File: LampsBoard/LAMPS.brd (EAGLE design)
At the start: 101.6 x 53.3 mm, 49 parts, among them IC1 LM358N, IC2 LM358N, IC3 5V, IC4 78L12Z, IC5 78L12Z, Q1 TIP120

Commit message: More work...
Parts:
- removed IC2: LM358N, linear:DIL08
- removed U$3: FIDUCIALMOUNT, SmartPrj:FIDUCIA-MOUNT
- removed X, Y: (no value), pinhead:1X01
- added 12V-AUX: (no value), SparkFun:1X02
- added 3.3V, 5V, VCC: (no value), adafruit:1X01
- added ADCH1: 8-15, pinhead:1X08
- added AUX1, COMM: 14-21, pinhead:1X08
- added F3: MFR500, RepRapjr:MFR500
- added IC6: UA741P, linear:DIL08
- added JP7: 22-37, pinhead:2X08
- added R4, R5, R6, R7: 5K, SparkFun:AXIAL-0.3
- added S2: (no value), switch-omron:B3F-31XX
- added X-GALVO, Y-GALVO: 22-23-2031, con-molex:22-23-2031
- added X1: MSTBA2, con-phoenix-508:MSTBA2
- IC1: value LM358N -> UA741P
- moved IC1 18.4 mm to (45.1, 27.3), turned to 270 degrees
- moved C6 10.8 mm to (62.9, 18.4)
- moved IC5 10.2 mm to (18.4, 17.1)
- moved C7 10.2 mm to (57.8, 23.5)
- moved C4 6.75 mm to (52.1, 24.8), turned to 270 degrees
- moved C14 6.25 mm to (12.7, 16.5)
- moved C3 3.81 mm to (57.1, 29.8)
- moved C13 1.91 mm to (12.7, 21.6)
- moved Z-MOT 1.91 mm to (76.2, 19.1)
- moved C12 1.27 mm to (12.7, 26.7)
- moved C1 1.27 mm to (57.1, 41.3)
- moved C2 0.63 mm to (57.1, 35.6), turned to 0 degrees
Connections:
- removed net V+: IC1.8, IC2.8
- removed net V-: IC1.4, IC2.4
- new net +12V: 12V-AUX.1, C10.1, C12.1, C13.1, F3.1, IC3.IN, IC4.3, IC5.3, Z-AXIS.VMOT
- new net N$27: IC6.4, X-GALVO.3
- new net N$28: IC6.7, X-GALVO.1
- new net N$29: COMM.2, COMMUNICATION.2
- new net N$30: R7.P$1
- new net N$31: IC1.6, R6.P$2, Y-GALVO.2
- new net N$32: IC1.4, Y-GALVO.3
- new net N$33: IC1.7, Y-GALVO.1
- new net N$34: IC1.3
- new net N$35: COMM.3, COMMUNICATION.3
- new net N$36: F3.2, X1.1
- new net N$37: COMM.4, COMMUNICATION.4
- new net N$38: COMM.5
- new net N$39: COMM.6, COMMUNICATION.6
- new net N$40: COMM.7, COMMUNICATION.7
- new net N$41: COMM.8, COMMUNICATION.8
- new net N$42: ADCH.1, ADCH1.1
- new net N$43: ADCH1.2
- new net N$44: ADCH.3, ADCH1.3
- new net N$45: ADCH.4, ADCH1.4
- new net N$46: ADCH.5, ADCH1.5
- new net N$47: ADCH.6, ADCH1.6
- new net N$48: ADCH.7, ADCH1.7
- new net N$49: ADCH.8, ADCH1.8
- new net N$50: JP1.15, JP7.15
- new net N$51: JP1.16, JP7.16
- new net N$52: JP1.13, JP7.13
- new net N$53: JP1.14, JP7.14
- new net N$54: JP1.11, JP7.11
- new net N$55: JP1.12, JP7.12
- new net N$56: JP1.9, JP7.9
- new net N$57: JP1.10, JP7.10
- new net N$58: JP1.7, JP7.7
- new net N$59: JP1.8, JP7.8
- new net N$60: JP1.5, JP7.5
- new net N$61: JP1.6, JP7.6
- new net N$62: JP1.3, JP7.3
- new net N$63: JP1.4, JP7.4
- new net N$64: JP1.1, JP7.1
- new net N$65: JP1.2, JP7.2
- new net N$74: AUX1.1, PWML.1
- new net N$75: AUX1.2, PWML.2
- new net N$76: AUX1.3, PWML.3
- new net N$77: AUX1.4, PWML.4
- new net N$78: AUX1.5, PWML.5
- new net N$79: AUX1.6, PWML.6
- new net N$80: AUX1.7, PWML.7
- new net RESET: POWER.1, S2.2
- net GND: now also 12V-AUX.2, AUX1.8, IC1.2, IC6.2, POWER.4, POWER.5, R4.P$1, R5.P$2, R6.P$1, R7.P$2, S2.1, X1.2
- net N$10: now also 5V.1, POWER.3; no longer IC2.1, IC2.2, Y.1
- net N$5: now also IC6.3; no longer IC1.3
- net N$6: now also R5.P$1
- net N$7: now also IC6.6, R4.P$2, X-GALVO.2; no longer IC1.1, IC1.2, X.1
- net N$8: now also 3.3V.1, POWER.2; no longer AD420ARZ1.17, IC2.3
- net N$9: now also COMM.1, COMMUNICATION.1; no longer AD420ARZ1.14, AD420ARZ1.15
- net VCC: now also VCC.1; no longer C10.1, C12.1, C13.1, IC3.IN, IC4.3, IC5.3, Z-AXIS.VMOT
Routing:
- net +12V: track 0.00 -> 155.7 mm
- net N$52: track 0.00 -> 100.1 mm, vias 0 -> 2
- net N$56: track 0.00 -> 78.8 mm, vias 0 -> 2
- net N$28: track 0.00 -> 68.6 mm
- net N$58: track 0.00 -> 68.1 mm
- net N$60: track 0.00 -> 67.5 mm, vias 0 -> 1
- net N$31: track 0.00 -> 59.8 mm, vias 0 -> 1
- net N$33: track 0.00 -> 51.5 mm, vias 0 -> 1
- net VCC: track 185.4 -> 136.3 mm, vias 0 -> 2
- net N$10: track 45.8 -> 5.08 mm, vias 1 -> 0
- net N$32: track 0.00 -> 35.5 mm
- net N$8: track 20.7 -> 55.2 mm, vias 0 -> 1
- net N$27: track 0.00 -> 33.8 mm
- net N$54: track 0.00 -> 27.8 mm, vias 0 -> 1
- net N$36: track 0.00 -> 19.9 mm, vias 0 -> 1
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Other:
- outline, holes or cut-outs redrawn
- board text removed: "22"
- board text removed: "24"
- board text removed: "26"
- board text removed: "28"
- board text removed: "30"
- board text removed: "31"
- board text removed: "32"
- board text removed: "33"
- board text removed: "34"
- board text removed: "35"
- board text removed: "36"
- board text removed: "37"
- board text removed: "38"
- board text removed: "39"
- board text removed: "40"
- board text removed: "41"
- board text removed: "42"
- board text removed: "43"
- board text removed: "44"
- board text removed: "45"
- board text removed: "46"
- board text removed: "47"
- board text removed: "48"
- board text removed: "49"
- board text removed: "50"
- board text removed: "51"
- board text removed: "52"
- board text removed: "53"
- board text removed: "ANALOG IN"
- board text removed: "DIGITAL"
- board text removed: "Galvos"
- board text removed: "PWM"
- board text removed: "RX1"
- board text removed: "RX2"
- board text removed: "RX3"
- board text removed: "SDA"
- board text removed: "TX1"
- board text removed: "TX2"
- board text removed: "TX3"

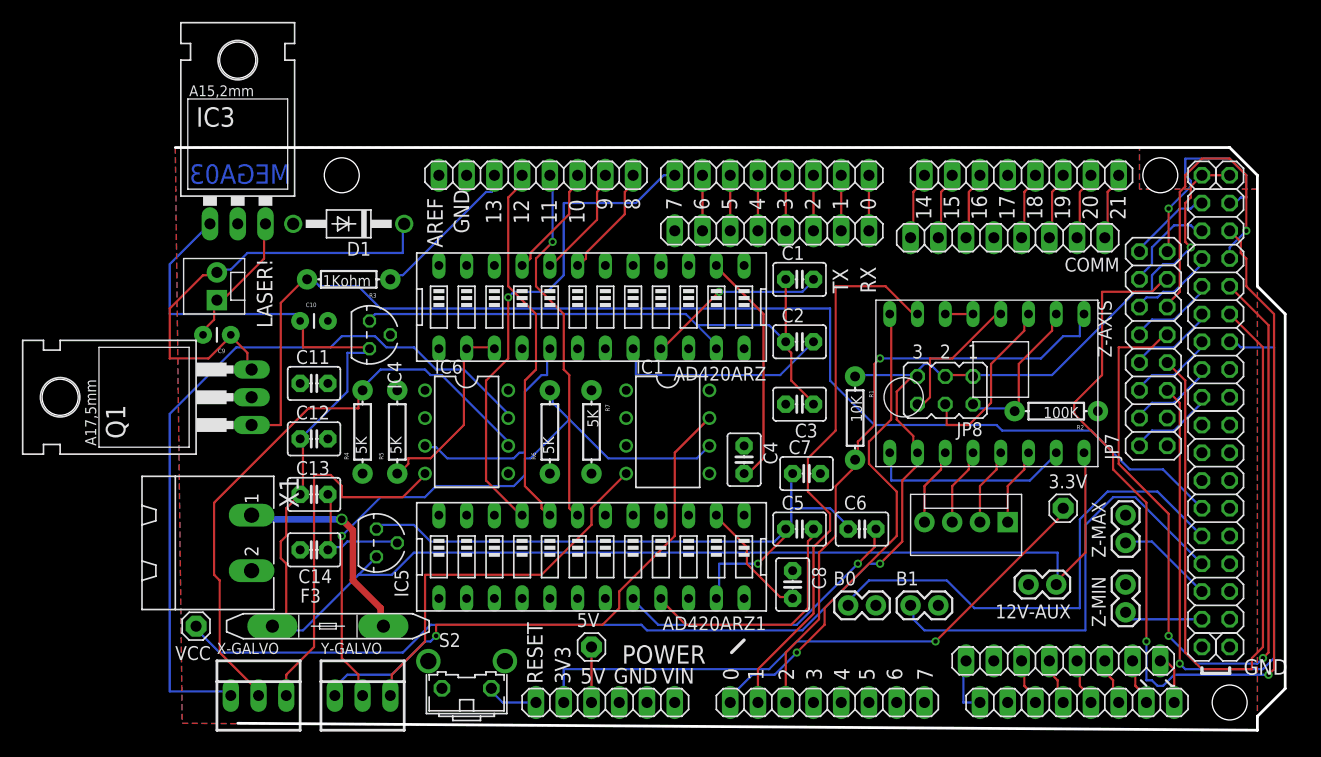
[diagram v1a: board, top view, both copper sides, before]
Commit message: Switching AD420 Chip mount
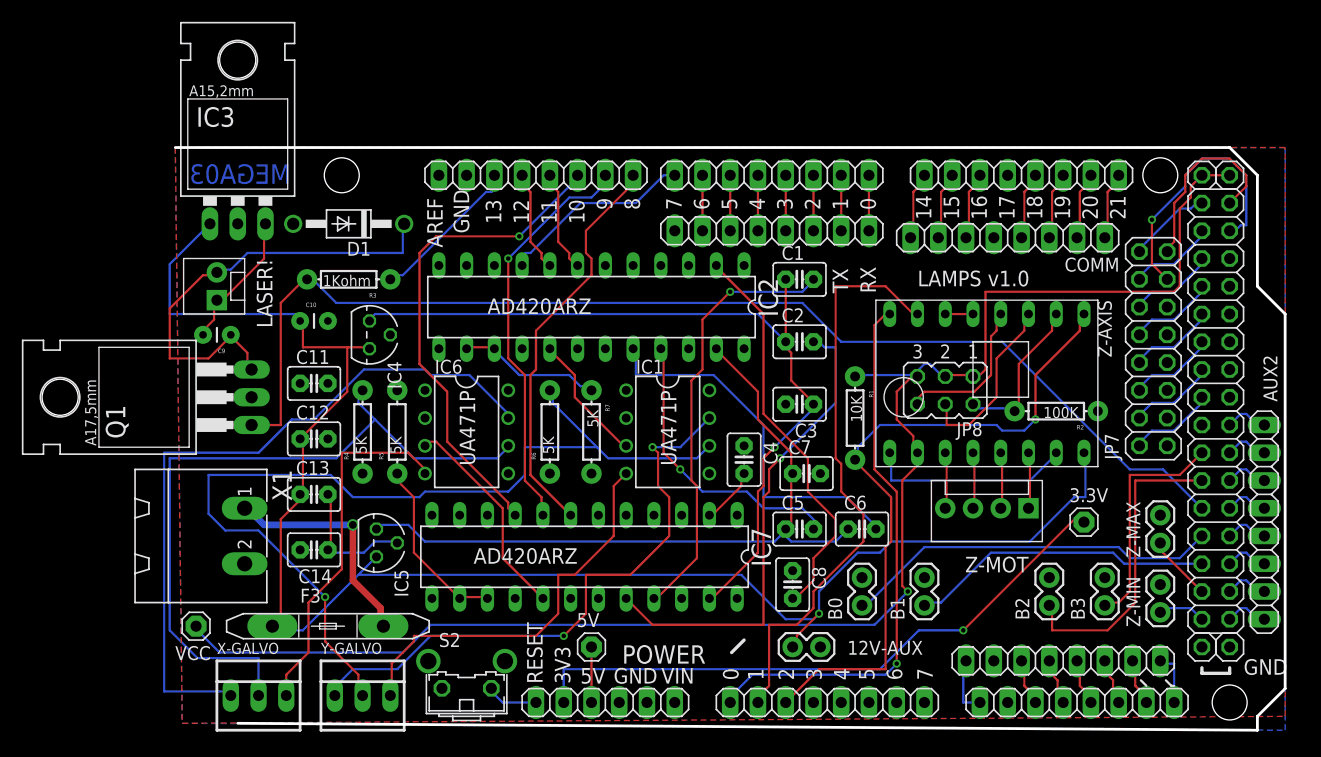
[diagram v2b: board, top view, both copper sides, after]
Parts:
- removed AD420ARZ, AD420ARZ1: (no value), special:EDG-12
- added AUX2: 14-21, pinhead:1X08
- added B2, B3: (no value), SparkFun:1X02
- added IC2, IC7: AD420ARZ, ic-package:DIL24-3
- moved 12V-AUX 24.8 mm to (56.5, 7.62), turned to 0 degrees
- moved Z-MAX 3.17 mm to (90.2, 17.1)
- moved Z-MIN 3.17 mm to (90.2, 10.8)
- moved 3.3V 2.29 mm to (83.2, 19.1)
- moved Z-MOT 2.29 mm to (78.1, 20.3)
- moved B0 1.27 mm to (62.9, 11.4), turned to 90 degrees
- moved B1 1.27 mm to (68.6, 11.4), turned to 90 degrees
- moved X1 0.90 mm to (1.27, 17.8)
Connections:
- new net D40: B3.1, JP2.14
- new net D42: B2.1, JP2.12
- new net N$66: AUX2.1, JP2.15
- new net N$67: AUX2.2, JP2.13
- new net N$68: AUX2.3, JP2.11
- new net N$69: AUX2.4, JP2.9
- new net N$70: AUX2.5, JP2.7
- new net N$71: AUX2.6, JP2.5
- new net N$72: AUX2.7, JP2.3
- new net N$73: AUX2.8, JP2.1
- net D10: now also IC7.9; no longer AD420ARZ.9
- net D11: now also IC2.7; no longer AD420ARZ1.7
- net D12: now also IC2.8; no longer AD420ARZ1.8
- net D7: now also IC2.9; no longer AD420ARZ1.9
- net D8: now also IC7.7; no longer AD420ARZ.7
- net D9: now also IC7.8; no longer AD420ARZ.8
- net GND: now also B2.2, B3.2, IC2.11, IC2.4, IC2.5, IC2.6, IC7.11, IC7.4, IC7.5, IC7.6; no longer AD420ARZ.11, AD420ARZ.4, AD420ARZ.5, AD420ARZ.6, AD420ARZ1.11, AD420ARZ1.4, AD420ARZ1.5, AD420ARZ1.6
- net N$1: now also IC2.21; no longer AD420ARZ1.21
- net N$18: now also IC7.23; no longer AD420ARZ.23
- net N$19: now also IC7.2; no longer AD420ARZ.2
- net N$2: now also IC2.20; no longer AD420ARZ1.20
- net N$24: now also IC2.2; no longer AD420ARZ1.2
- net N$25: now also IC2.23; no longer AD420ARZ1.23
- net N$3: now also IC7.21; no longer AD420ARZ.21
- net N$30: now also IC2.14, IC2.15
- net N$34: now also IC2.17
- net N$4: now also IC7.20; no longer AD420ARZ.20
- net N$5: now also IC7.17; no longer AD420ARZ.17
- net N$6: now also IC7.14, IC7.15; no longer AD420ARZ.14, AD420ARZ.15
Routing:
- net N$56: track 78.8 -> 0.00 mm, vias 2 -> 0
- net N$52: track 100.1 -> 24.5 mm, vias 2 -> 1
- net N$58: track 68.1 -> 0.00 mm
- net N$60: track 67.5 -> 0.00 mm, vias 1 -> 0
- net D10: track 10.6 -> 45.6 mm, vias 0 -> 1
- net D42: track 0.00 -> 28.3 mm
- net D7: track 45.9 -> 18.0 mm, vias 1 -> 0
- net N$54: track 27.8 -> 0.00 mm, vias 1 -> 0
- net D9: track 10.6 -> 37.5 mm, vias 0 -> 1
- net D8: track 10.6 -> 37.1 mm
- net N$31: track 59.8 -> 85.8 mm
- net N$24: track 11.1 -> 36.7 mm
- net D12: track 34.3 -> 9.51 mm
- net D11: track 33.6 -> 9.51 mm, vias 1 -> 0
- net N$4: track 20.0 -> 44.0 mm, vias 0 -> 1
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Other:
- board text added: "AD420ARZ"
- board text added: "LAMPS v1.0"
- board text added: "UA471P"
- board text added: "Z-MOT"

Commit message: movin
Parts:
- removed JP7: 22-37, pinhead:2X08
- removed X1: MSTBA2, con-phoenix-508:MSTBA2
- added 12V: MSTBA2, con-phoenix-508:MSTBA2
- IC2, IC7: value AD420ARZ -> (none); device ic-package:DIL24-3 -> ic-package:DIL24-6
- moved 12V-AUX 54.9 mm to (1.91, 1.91), turned to 90 degrees
- moved 5V 50.9 mm to (88.9, 10.8)
- moved IC6 42.6 mm to (68.6, 19.7), turned to 0 degrees
- moved IC1 37.0 mm to (81.3, 19.7), turned to 0 degrees
- moved C7 30.8 mm to (27.3, 19.1)
- moved C5 30.4 mm to (27.3, 24.1)
- moved C8 29.2 mm to (27.3, 12.7), turned to 180 degrees
- moved 3.3V 28.6 mm to (81.3, 47.6), turned to 180 degrees
- moved C4 27.2 mm to (68.6, 46.4), turned to 180 degrees
- moved Z-MOT 19.7 mm to (88.9, 36.8), turned to 270 degrees
- moved C6 18.3 mm to (56.5, 35.6), turned to 270 degrees
- moved R7 17.9 mm to (22.2, 19.1)
- moved R6 17.5 mm to (22.2, 40.0), turned to 270 degrees
- moved R1 16.9 mm to (78.7, 32.4), turned to 0 degrees
- moved Z-MIN 8.28 mm to (90.8, 19.1), turned to 180 degrees
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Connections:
- removed net N$50: JP1.15, JP7.15
- removed net N$51: JP1.16, JP7.16
- removed net N$52: JP1.13, JP7.13
- removed net N$53: JP1.14, JP7.14
- removed net N$54: JP1.11, JP7.11
- removed net N$55: JP1.12, JP7.12
- removed net N$56: JP1.9, JP7.9
- removed net N$57: JP1.10, JP7.10
- removed net N$58: JP1.7, JP7.7
- removed net N$59: JP1.8, JP7.8
- removed net N$60: JP1.5, JP7.5
- removed net N$61: JP1.6, JP7.6
- removed net N$62: JP1.3, JP7.3
- removed net N$63: JP1.4, JP7.4
- removed net N$64: JP1.1, JP7.1
- removed net N$65: JP1.2, JP7.2
- net GND: now also 12V.2; no longer X1.2
- net N$36: now also 12V.1; no longer X1.1
- net N$38: now also COMMUNICATION.5
- net N$43: now also ADCH.2
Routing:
- net N$34: track 12.0 -> 66.6 mm, vias 0 -> 2
- net N$10: track 5.08 -> 55.8 mm
- net N$33: track 54.6 -> 100.5 mm, vias 2 -> 1
- net N$32: track 36.7 -> 78.5 mm
- net N$27: track 33.0 -> 66.8 mm, vias 0 -> 3
- net N$7: track 66.4 -> 97.4 mm, vias 0 -> 1
- net N$52: track 24.5 -> 0.00 mm, vias 1 -> 0
- net N$19: track 5.29 -> 27.9 mm
- net N$23: track 5.33 -> 24.6 mm, vias 0 -> 1
- net N$8: track 57.5 -> 76.6 mm
- net +12V: track 154.8 -> 172.9 mm
- net N$2: track 34.3 -> 16.3 mm, vias 0 -> 1
- net N$24: track 36.7 -> 54.4 mm, vias 0 -> 2
- net N$50: track 17.7 -> 0.00 mm
- net N$22: track 5.33 -> 22.3 mm
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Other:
- board size 101.6 x 53.3 mm -> 102.2 x 53.3 mm
- board text added: "7805"
- board text added: "HAWKINSOFT LLC c 2012"
- board text added: "TIP120"
- board text removed: "10"
- board text removed: "11"
- board text removed: "12"
- board text removed: "13"
- board text removed: "14"
- board text removed: "15"
- board text removed: "16"
- board text removed: "17"
- board text removed: "18"
- board text removed: "19"
- board text removed: "20"
- board text removed: "21"
- board text removed: "8"
- board text removed: "9"
- board text removed: "MEGA03"
